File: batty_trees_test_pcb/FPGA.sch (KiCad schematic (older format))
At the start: 2 parts

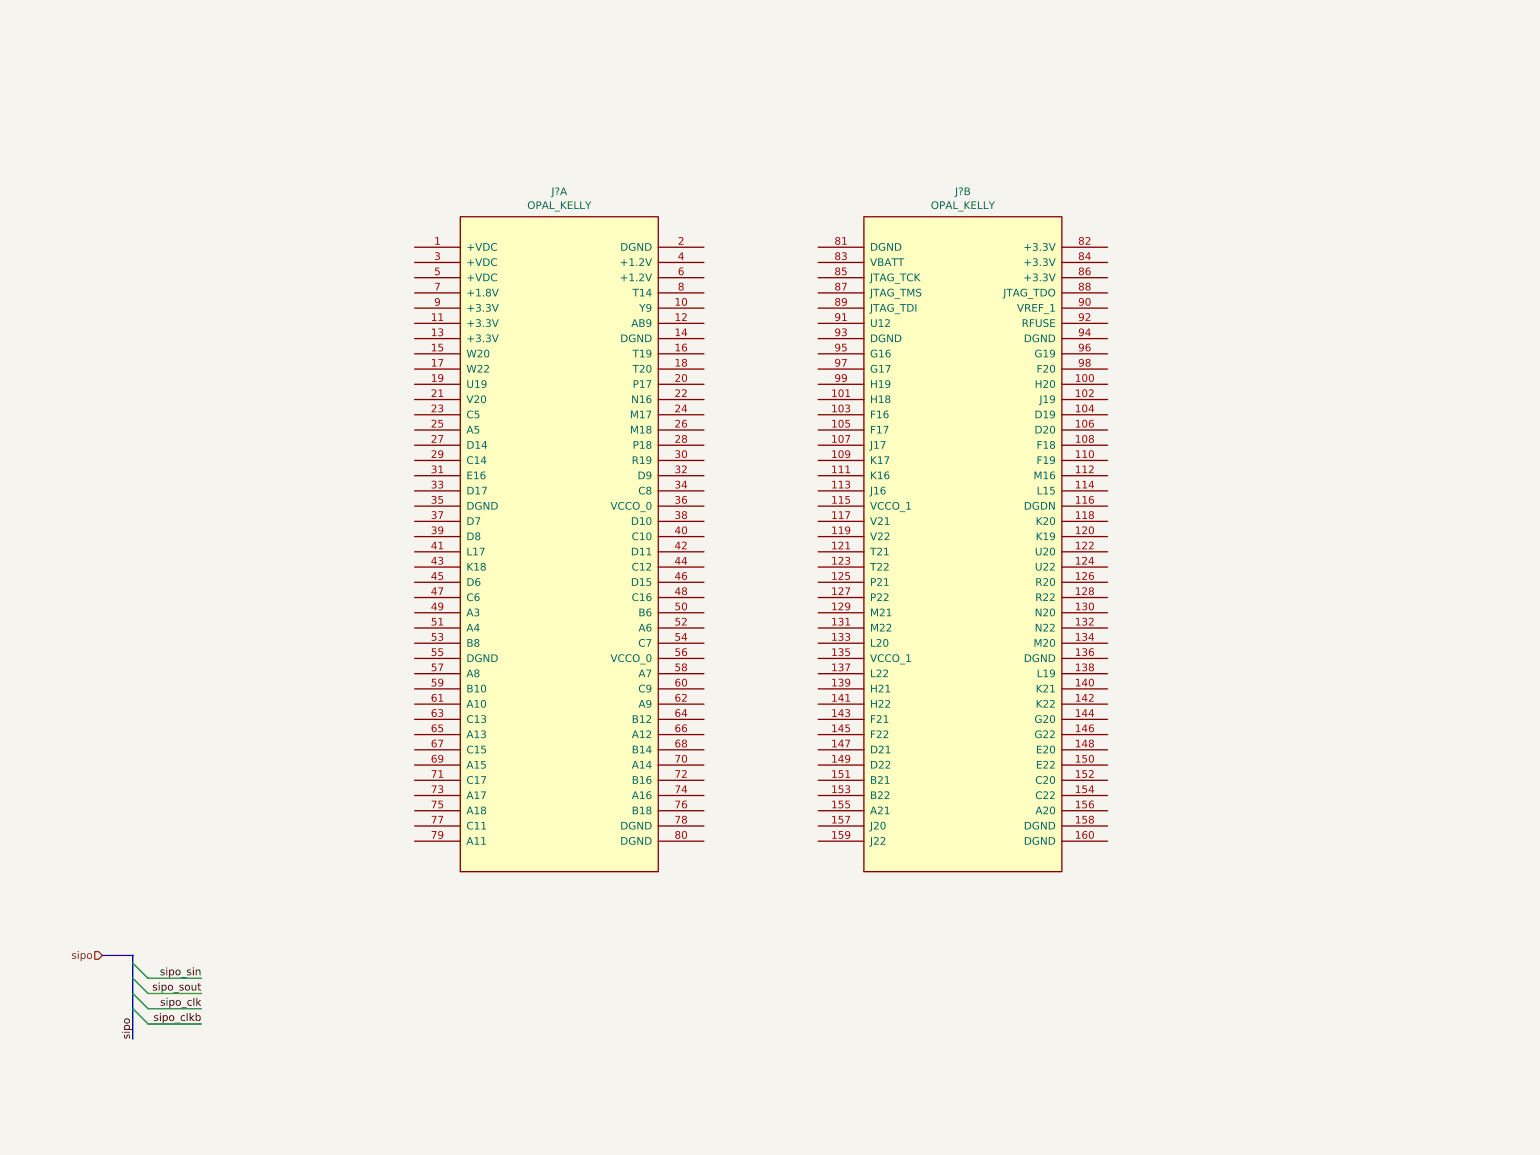
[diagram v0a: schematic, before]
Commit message: wired up chip to fpga on schematic and begininng to do layout
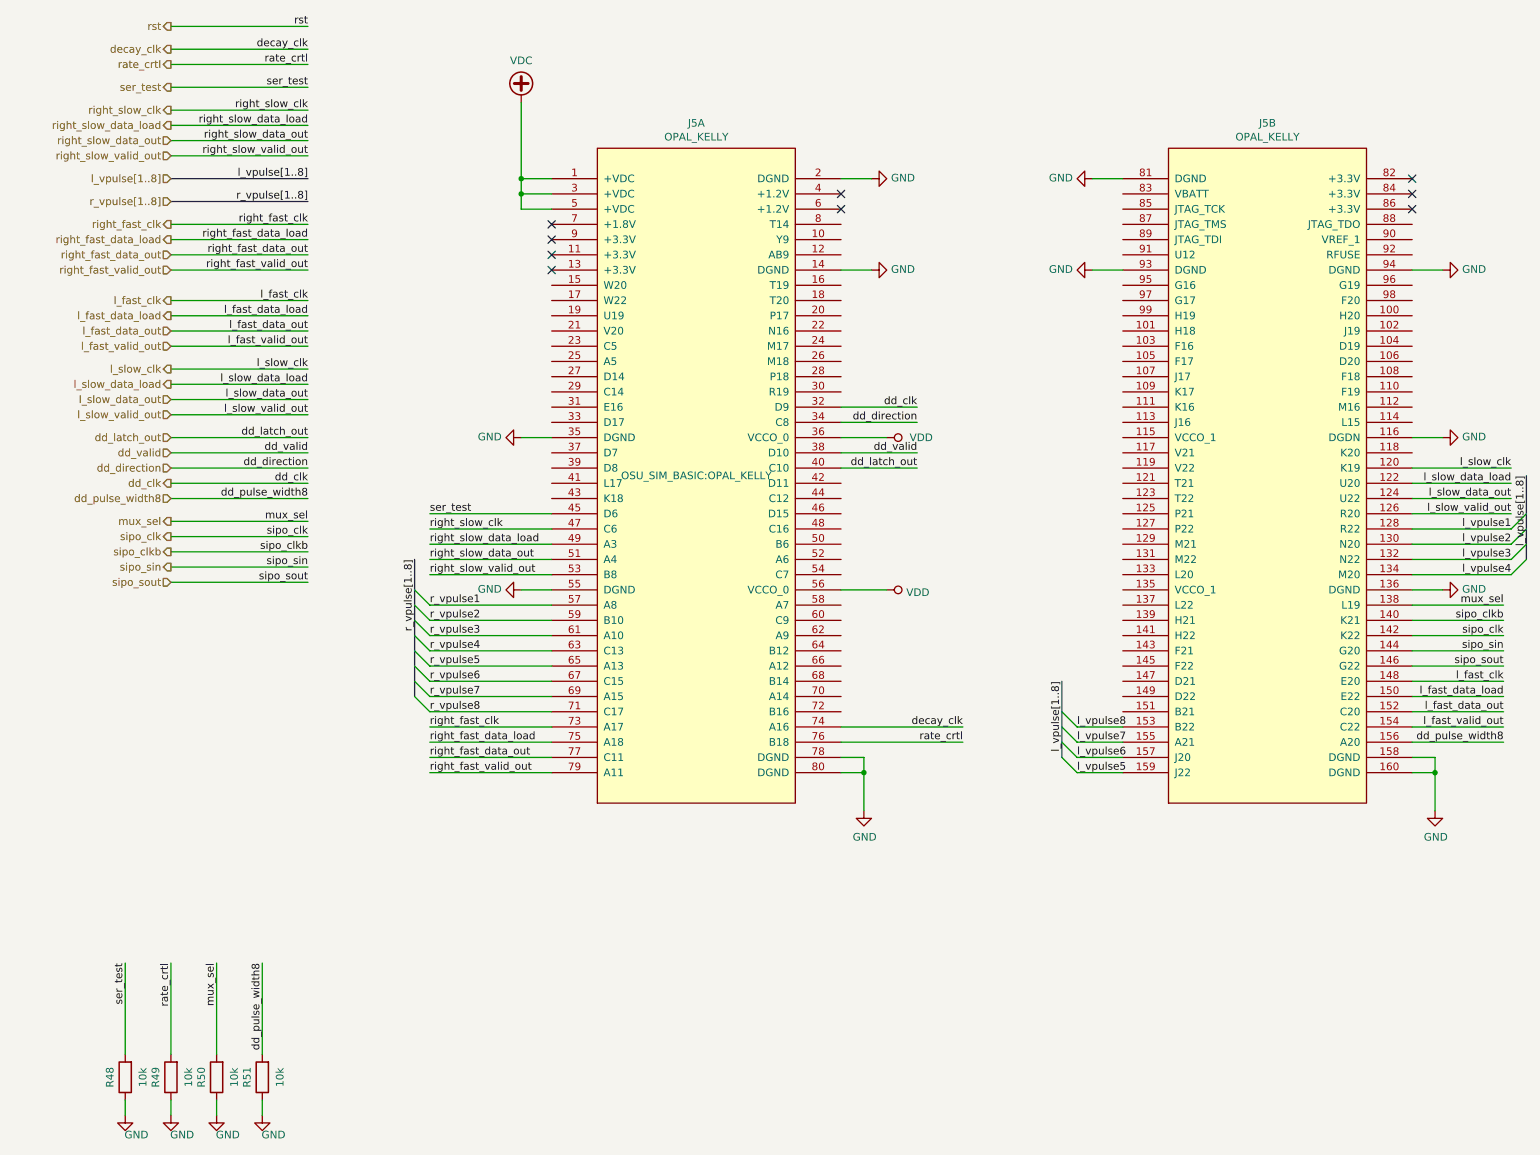
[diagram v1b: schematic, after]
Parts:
- added R48, R49, R50, R51: 10k, Resistor_SMD:R_0805_2012Metric_Pad1.15x1.40mm_HandSolder, symbol Device:R
- J5: renamed from J?; footprint MODULE -> OSU_SIM_BASIC:OPAL_KELLY
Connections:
- net sipo_clk: now also J5.142 (K22)
- net sipo_clkb: now also J5.140 (K21)
- net sipo_sin: now also J5.144 (G20)
- net sipo_sout: now also J5.146 (G22)
- net VDC: now reaches J5.1 (+VDC)
- net VDC: now also J5.3 (+VDC), J5.5 (+VDC)
- net GND: now reaches J5.14 (DGND)
- net GND: now also J5.116 (DGDN), J5.136 (DGND), J5.158 (DGND), J5.160 (DGND), J5.2 (DGND), J5.35 (DGND), J5.55 (DGND), J5.78 (DGND), J5.80 (DGND), J5.81 (DGND), J5.93 (DGND), J5.94 (DGND), R48.1, R49.1, R50.1, R51.1
- net dd_clk: now reaches J5.32 (D9)
- net dd_direction: now reaches J5.34 (C8)
- net VDD: now reaches J5.36 (VCCO_0)
- net VDD: now also J5.56 (VCCO_0)
- net dd_valid: now reaches J5.38 (D10)
- net dd_latch_out: now reaches J5.40 (C10)
- net ser_test: now reaches J5.45 (D6)
- net ser_test: now also R48.2
- net right_slow_clk: now reaches J5.47 (C6)
- net right_slow_data_load: now reaches J5.49 (A3)
- net right_slow_data_out: now reaches J5.51 (A4)
- net right_slow_valid_out: now reaches J5.53 (B8)
- net r_vpulse1: now reaches J5.57 (A8)
- net r_vpulse2: now reaches J5.59 (B10)
- net r_vpulse3: now reaches J5.61 (A10)
- net r_vpulse4: now reaches J5.63 (C13)
- net r_vpulse5: now reaches J5.65 (A13)
- net r_vpulse6: now reaches J5.67 (C15)
- net r_vpulse7: now reaches J5.69 (A15)
- net r_vpulse8: now reaches J5.71 (C17)
- net right_fast_clk: now reaches J5.73 (A17)
- net decay_clk: now reaches J5.74 (A16)
- net right_fast_data_load: now reaches J5.75 (A18)
- net rate_crtl: now reaches J5.76 (B18)
- net rate_crtl: now also R49.2
- net right_fast_data_out: now reaches J5.77 (C11)
- net right_fast_valid_out: now reaches J5.79 (A11)
- net l_slow_clk: now reaches J5.120 (K19)
- net l_slow_data_load: now reaches J5.122 (U20)
- net l_slow_data_out: now reaches J5.124 (U22)
- net l_slow_valid_out: now reaches J5.126 (R20)
- net l_vpulse1: now reaches J5.128 (R22)
- net l_vpulse2: now reaches J5.130 (N20)
- net l_vpulse3: now reaches J5.132 (N22)
- net l_vpulse4: now reaches J5.134 (M20)
- net mux_sel: now reaches J5.138 (L19)
- net mux_sel: now also R50.2
- net l_fast_clk: now reaches J5.148 (E20)
- net l_fast_data_load: now reaches J5.150 (E22)
- net l_fast_data_out: now reaches J5.152 (C20)
- net l_vpulse8: now reaches J5.153 (B22)
- net l_fast_valid_out: now reaches J5.154 (C22)
- net l_vpulse7: now reaches J5.155 (A21)
- net dd_pulse_width8: now reaches J5.156 (A20)
- net dd_pulse_width8: now also R51.2
- net l_vpulse6: now reaches J5.157 (J20)
- net l_vpulse5: now reaches J5.159 (J22)
- no-connect marks 0 -> 9
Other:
- moved on the sheet: J5A, J5B

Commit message: more layout work ~90% finished
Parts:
- added J10, J12, J5, J9: Conn_02x04_Odd_Even, Connector_PinHeader_2.54mm:PinHeader_2x04_P2.54mm_Vertical, symbol Connector_Generic:Conn_02x04_Odd_Even
- added J11: Conn_02x08_Odd_Even, Connector_PinHeader_2.54mm:PinHeader_2x08_P2.54mm_Vertical, symbol Connector_Generic:Conn_02x08_Odd_Even
- renumbered J5 to J13
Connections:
- net GND: now also J10.2 (Pin_2), J10.4 (Pin_4), J10.6 (Pin_6), J10.8 (Pin_8), J11.1 (Pin_1), J11.11 (Pin_11), J11.13 (Pin_13), J11.15 (Pin_15), J11.3 (Pin_3), J11.5 (Pin_5), J11.7 (Pin_7), J11.9 (Pin_9), J12.2 (Pin_2), J12.4 (Pin_4), J12.6 (Pin_6), J12.8 (Pin_8), J5.1 (Pin_1), J5.3 (Pin_3), J5.5 (Pin_5), J5.7 (Pin_7), J9.1 (Pin_1), J9.3 (Pin_3), J9.5 (Pin_5), J9.7 (Pin_7)
- net VDD: now also J13.115 (VCCO_1), J13.135 (VCCO_1)
- net dd_clk: now also J9.6 (Pin_6)
- net dd_direction: now also J9.8 (Pin_8)
- net dd_latch_out: now also J9.4 (Pin_4)
- net dd_valid: now also J9.2 (Pin_2)
- net l_slow_clk: now also J12.1 (Pin_1)
- net l_slow_data_load: now also J12.3 (Pin_3)
- net l_slow_data_out: now also J12.5 (Pin_5)
- net l_slow_valid_out: now also J12.7 (Pin_7)
- net l_vpulse1: now also J10.1 (Pin_1)
- net l_vpulse2: now also J10.3 (Pin_3)
- net l_vpulse3: now also J10.5 (Pin_5)
- net l_vpulse4: now also J10.7 (Pin_7)
- net l_vpulse5: now also J5.8 (Pin_8)
- net l_vpulse6: now also J5.6 (Pin_6)
- net l_vpulse7: now also J5.4 (Pin_4)
- net l_vpulse8: now also J5.2 (Pin_2)
- net r_vpulse1: now also J11.2 (Pin_2)
- net r_vpulse2: now also J11.4 (Pin_4)
- net r_vpulse3: now also J11.6 (Pin_6)
- net r_vpulse4: now also J11.8 (Pin_8)
- net r_vpulse5: now also J11.10 (Pin_10)
- net r_vpulse6: now also J11.12 (Pin_12)
- net r_vpulse7: now also J11.14 (Pin_14)
- net r_vpulse8: now also J11.16 (Pin_16)

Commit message: Layout finished and gerbers generated checking for DFM
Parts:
- added C35: 0.1uF, Capacitor_SMD:C_0805_2012Metric_Pad1.15x1.40mm_HandSolder, symbol Device:C_Small
- added R52: 1k, Resistor_SMD:R_0805_2012Metric_Pad1.15x1.40mm_HandSolder, symbol Device:R
- added R53: 100k, Resistor_SMD:R_0805_2012Metric_Pad1.15x1.40mm_HandSolder, symbol Device:R
- added S1: GPTS203211B, digikey-footprints:PushButton_12x12mm_THT_GPTS203211B, symbol dk_Pushbutton-Switches:GPTS203211B
- R48, R49, R51: Digi-Key_PN (none) -> 311-10.0KCRCT-ND
- R50: Digi-Key-PN (none) -> 311-10.0KCRCT-ND
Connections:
- net GND: now also C35.1, R53.1
- net VDD: now also R52.2
- net rst: now also J13.151 (B21), C35.2, R53.2, S1.2
- new net: R52.1, S1.1
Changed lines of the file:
@@
 F 2 "Resistor_SMD:R_0805_2012Metric_Pad1.15x1.40mm_HandSolder" V 980 7550 50  0001 C CNN
 F 3 "~" H 1050 7550 50  0001 C CNN
+F 4 "311-10.0KCRCT-ND" V 1050 7550 50  0001 C CNN "Digi-Key_PN"
 	1    1050 7550
 	-1   0    0    1
@@
 F 2 "Resistor_SMD:R_0805_2012Metric_Pad1.15x1.40mm_HandSolder" V 1280 7550 50  0001 C CNN
 F 3 "~" H 1350 7550 50  0001 C CNN
+F 4 "311-10.0KCRCT-ND" V 1350 7550 50  0001 C CNN "Digi-Key_PN"
 	1    1350 7550
 	-1   0    0    1
@@
 F 2 "Resistor_SMD:R_0805_2012Metric_Pad1.15x1.40mm_HandSolder" V 1580 7550 50  0001 C CNN
 F 3 "~" H 1650 7550 50  0001 C CNN
+F 4 "311-10.0KCRCT-ND" V 1650 7550 50  0001 C CNN "Digi-Key-PN"
 	1    1650 7550
 	-1   0    0    1
@@
 F 2 "Resistor_SMD:R_0805_2012Metric_Pad1.15x1.40mm_HandSolder" V 1880 7550 50  0001 C CNN
 F 3 "~" H 1950 7550 50  0001 C CNN
+F 4 "311-10.0KCRCT-ND" V 1950 7550 50  0001 C CNN "Digi-Key_PN"
 	1    1950 7550
 	-1   0    0    1
@@
 Wire Wire Line
 	7150 4350 7600 4350
+$Comp
+L dk_Pushbutton-Switches:GPTS203211B S1
+U 1 1 5F8A1849
+P 1350 5750
+F 0 "S1" H 1350 6025 50  0000 C CNN
+F 1 "GPTS203211B" H 1350 5934 50  0000 C CNN
+F 2 "digikey-footprints:PushButton_12x12mm_THT_GPTS203211B" H 1550 5950 50  0001 L CNN
+F 3 "http://switches-connectors-custom.cwind.com/Asset/GPTS203211BR2.pdf" H 1550 6050 60  0001 L CNN
+F 4 "CW181-ND" H 1550 6150 60  0001 L CNN "Digi-Key_PN"
+F 5 "GPTS203211B" H 1550 6250 60  0001 L CNN "MPN"
+F 6 "Switches" H 1550 6350 60  0001 L CNN "Category"
+F 7 "Pushbutton Switches" H 1550 6450 60  0001 L CNN "Family"
+F 8 "http://switches-connectors-custom.cwind.com/Asset/GPTS203211BR2.pdf" H 1550 6550 60  0001 L CNN "DK_Datasheet_Link"
+F 9 "/product-detail/en/cw-industries/GPTS203211B/CW181-ND/3190590" H 1550 6650 60  0001 L CNN "DK_Detail_Page"
+F 10 "SWITCH PUSHBUTTON SPST 1A 30V" H 1550 6750 60  0001 L CNN "Description"
+F 11 "CW Industries" H 1550 6850 60  0001 L CNN "Manufacturer"
+F 12 "Active" H 1550 6950 60  0001 L CNN "Status"
+	1    1350 5750
+	1    0    0    -1
+$EndComp
+Wire Wire Line
+	900  5750 1150 5750
+$Comp
+L power:VDD #PWR0170
+U 1 1 5F8AFBE8
+P 900 5200
+F 0 "#PWR0170" H 900 5050 50  0001 C CNN
+F 1 "VDD" H 917 5373 50  0000 C CNN
+F 2 "" H 900 5200 50  0001 C CNN
+F 3 "" H 900 5200 50  0001 C CNN
+	1    900  5200
+	1    0    0    -1
+$EndComp
+Wire Wire Line
+	1550 5750 1700 5750
+Wire Wire Line
+	1700 5750 1700 5850
+$Comp
+L power:GND #PWR0171
+U 1 1 5F8D63C9
+P 1700 6200
+F 0 "#PWR0171" H 1700 5950 50  0001 C CNN
+F 1 "GND" H 1705 6072 50  0000 R CNN
+F 2 "" H 1700 6200 50  0001 C CNN
+F 3 "" H 1700 6200 50  0001 C CNN
+	1    1700 6200
+	-1   0    0    -1
+$EndComp
+Wire Wire Line
+	1700 6200 1700 6050
+Connection ~ 1700 5750
+Wire Wire Line
+	7600 5150 7300 5150
+Text Label 7300 5150 0    50   ~ 0
+rst
+$Comp
+L Device:C_Small C?
+U 1 1 5F8BF79C
+P 1700 5950
+AR Path="/5F3A707E/5F8BF79C" Ref="C?"  Part="1"
+AR Path="/5F370A72/5F8BF79C" Ref="C?"  Part="1"
+AR Path="/5F35DB40/5F8BF79C" Ref="C35"  Part="1"
+F 0 "C35" H 1608 5996 50  0000 R CNN
+F 1 "0.1uF" H 1608 5905 50  0000 R CNN
+F 2 "Capacitor_SMD:C_0805_2012Metric_Pad1.15x1.40mm_HandSolder" H 1700 5950 50  0001 C CNN
+F 3 "~" H 1700 5950 50  0001 C CNN
+F 4 "399-8000-1-ND" H 1700 5950 50  0001 C CNN "Digi-Key_PN"
+	1    1700 5950
+	1    0    0    1
+$EndComp
+Wire Wire Line
+	1700 5750 1900 5750
+Text Label 2000 5750 2    50   ~ 0
+rst
+Wire Wire Line
+	900  5200 900  5350
+Wire Wire Line
+	900  5650 900  5750
+$Comp
+L Device:R R?
+U 1 1 5F8A2FD8
+P 900 5500
+AR Path="/5F370A72/5F8A2FD8" Ref="R?"  Part="1"
+AR Path="/5F35DB40/5F8A2FD8" Ref="R52"  Part="1"
+F 0 "R52" V 1000 5500 50  0000 C CNN
+F 1 "1k" V 784 5500 50  0000 C CNN
+F 2 "Resistor_SMD:R_0805_2012Metric_Pad1.15x1.40mm_HandSolder" V 830 5500 50  0001 C CNN
+F 3 "~" H 900 5500 50  0001 C CNN
+F 4 "311-1.0KARCT-ND" V 900 5500 50  0001 C CNN "Digi-Key-PN"
+	1    900  5500
+	-1   0    0    1
+$EndComp
+$Comp
+L Device:R R?
+U 1 1 5F94E7EF
+P 1900 6000
+AR Path="/5F370A72/5F94E7EF" Ref="R?"  Part="1"
+AR Path="/5F35DB40/5F94E7EF" Ref="R53"  Part="1"
+F 0 "R53" V 1693 6000 50  0000 C CNN
+F 1 "100k" V 1784 6000 50  0000 C CNN
+F 2 "Resistor_SMD:R_0805_2012Metric_Pad1.15x1.40mm_HandSolder" V 1830 6000 50  0001 C CNN
+F 3 "~" H 1900 6000 50  0001 C CNN
+F 4 "311-100KCRCT-ND" V 1900 6000 50  0001 C CNN "Digi-Key_PN"
+	1    1900 6000
+	-1   0    0    1
+$EndComp
+Wire Wire Line
+	1900 5850 1900 5750
+Connection ~ 1900 5750
+Wire Wire Line
+	1900 5750 2000 5750
+$Comp
+L power:GND #PWR0172
+U 1 1 5F97E1A2
+P 1900 6200
+F 0 "#PWR0172" H 1900 5950 50  0001 C CNN
+F 1 "GND" H 1905 6072 50  0000 R CNN
+F 2 "" H 1900 6200 50  0001 C CNN
+F 3 "" H 1900 6200 50  0001 C CNN
+	1    1900 6200
+	-1   0    0    -1
+$EndComp
+Wire Wire Line
+	1900 6200 1900 6150
 Wire Bus Line
 	10250 3600 10250 4150

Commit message: all componenets updated with digikey pn bom generated
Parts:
- R52: Digi-Key-PN 311-1.0KARCT-ND -> 311-1.00KCRCT-ND
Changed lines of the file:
@@
 F 2 "Resistor_SMD:R_0805_2012Metric_Pad1.15x1.40mm_HandSolder" V 830 5500 50  0001 C CNN
 F 3 "~" H 900 5500 50  0001 C CNN
-F 4 "311-1.0KARCT-ND" V 900 5500 50  0001 C CNN "Digi-Key-PN"
+F 4 "311-1.00KCRCT-ND" V 900 5500 50  0001 C CNN "Digi-Key-PN"
 	1    900  5500
 	-1   0    0    1
